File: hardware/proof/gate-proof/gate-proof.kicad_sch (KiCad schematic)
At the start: 4 parts, among them J1 MAINS_IN, J2 LV_IN

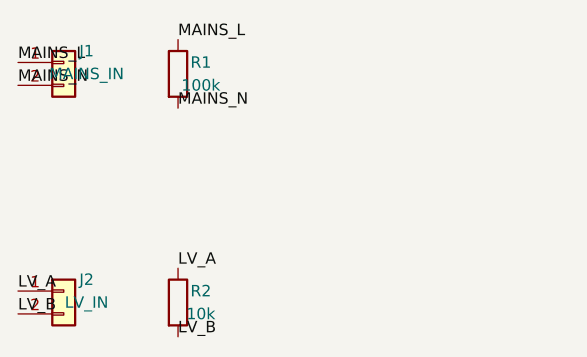
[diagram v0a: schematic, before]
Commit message: feat(hardware): check a board's connectivity against its pin allocation record, each fault proven on a throwaway design [SOL-HW-CONNECTIVITY-CHECK.C1, .C2, .C3, .C4, .C5]
Co-Authored-By: Claude Sonnet 5.5 <noreply@anthropic.com>
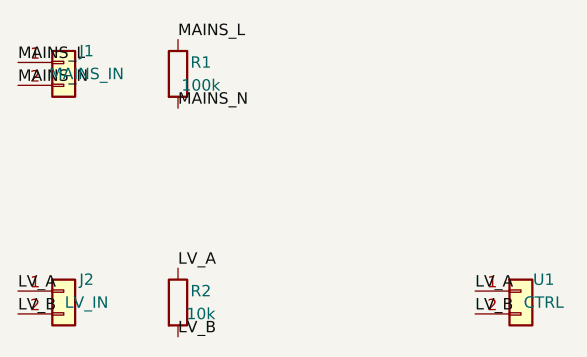
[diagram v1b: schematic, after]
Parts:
- added U1: CTRL, proof:Controller_1x02, symbol proof:Controller
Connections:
- net LV_A: now also U1.1 (PA0)
- net LV_B: now also U1.2 (PA1)
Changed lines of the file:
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@@
+		)
+	)
+	(label "LV_A"
+		(at 96.52 76.2 0)
+		(effects
+			(font
+				(size 1.27 1.27)
+			)
+			(justify left bottom)
+		)
+	)
+	(label "LV_B"
+		(at 96.52 78.74 0)
+		(effects
+			(font
+				(size 1.27 1.27)
+			)
+			(justify left bottom)
+		)
+	)
+	(symbol
+		(lib_id "proof:Controller")
+		(at 101.6 76.2 0)
+		(unit 1)
+		(body_style 1)
+		(exclude_from_sim no)
+		(in_bom yes)
+		(on_board yes)
+		(in_pos_files yes)
+		(dnp no)
+		(property "Reference" "U1"
+			(at 104.14 74.93 0)
+			(effects
+				(font
+					(size 1.27 1.27)
+				)
+			)
+		)
+		(property "Value" "CTRL"
+			(at 104.14 77.47 0)
+			(effects
+				(font
+					(size 1.27 1.27)
+				)
+			)
+		)
+		(property "Footprint" "proof:Controller_1x02"
+			(at 101.6 76.2 0)
+			(hide yes)
+			(effects
+				(font
+					(size 1.27 1.27)
+				)
+			)
+		)
+		(property "Datasheet" ""
+			(at 101.6 76.2 0)
+			(hide yes)
+			(effects
+				(font
+					(size 1.27 1.27)
+				)
+			)
+		)
+		(property "Description" ""
+			(at 101.6 76.2 0)
+			(hide yes)
+			(effects
+				(font
+					(size 1.27 1.27)
+				)
+			)
+		)
+		(pin "1"
+		)
+		(pin "2"
+		)
+		(instances
+			(project "gate-proof"
+				(path "/09ee335c-2898-46bc-9295-ebc68c9ce1e2"
+					(reference "U1")
+					(unit 1)
+				)
+			)
 		)
 	)

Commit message: feat(hardware): check a board's parts against its specification record and the dated catalogue extract, each fault proven on a throwaway design [SOL-HW-PARTS-CHECK.C1, .C2, .C3, .C4, .C5]
Co-Authored-By: Claude Sonnet 5.5 <noreply@anthropic.com>
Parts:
- J1: LCSC (none) -> C9000001
- J2: LCSC (none) -> C9000003
- R1: LCSC (none) -> C9000002; Rating (none) -> 0.25W
- R2: LCSC (none) -> C9000004; Rating (none) -> 0.25W
- U1: LCSC (none) -> C9000005
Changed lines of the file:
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@@
+			)
+		)
+		(property "LCSC" "C9000001"
+			(at 50.8 50.8 0)
+			(hide yes)
+			(effects
+				(font
+					(size 1.27 1.27)
+				)
 			)
 		)
@@
 			)
 		)
+		(property "LCSC" "C9000002"
+			(at 63.5 52.07 0)
+			(hide yes)
+			(effects
+				(font
+					(size 1.27 1.27)
+				)
+			)
+		)
+		(property "Rating" "0.25W"
+			(at 63.5 52.07 0)
+			(hide yes)
+			(effects
+				(font
+					(size 1.27 1.27)
+				)
+			)
+		)
 		(property "Datasheet" ""
 			(at 63.5 52.07 0)
@@
 			)
 		)
+		(property "LCSC" "C9000003"
+			(at 50.8 76.2 0)
+			(hide yes)
+			(effects
+				(font
+					(size 1.27 1.27)
+				)
+			)
+		)
 		(property "Datasheet" ""
 			(at 50.8 76.2 0)
@@
 			)
 		)
+		(property "LCSC" "C9000004"
+			(at 63.5 77.47 0)
+			(hide yes)
+			(effects
+				(font
+					(size 1.27 1.27)
+				)
+			)
+		)
+		(property "Rating" "0.25W"
+			(at 63.5 77.47 0)
+			(hide yes)
+			(effects
+				(font
+					(size 1.27 1.27)
+				)
+			)
+		)
 		(property "Datasheet" ""
 			(at 63.5 77.47 0)
@@
 			(at 101.6 76.2 0)
 			(hide yes)
+			(effects
+				(font
+					(size 1.27 1.27)
+				)
+			)
+		)
+		(property "LCSC" "C9000005"
+			(at 101.6 76.2 0)
+			(hide yes)

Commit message: feat(hardware): look nothing up for a position stated to have no catalogue number [SOL-PRE-ORDER-CHECK-PARTS-WITHOUT-CATALOGUE-NUMBER.C1, .C2]
Co-Authored-By: Claude Sonnet 5.5 <noreply@anthropic.com>
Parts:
- J2: LCSC C9000003 -> none
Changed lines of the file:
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@@
 			)
 		)
-		(property "LCSC" "C9000003"
+		(property "LCSC" "none"
 			(at 50.8 76.2 0)
 			(hide yes)
